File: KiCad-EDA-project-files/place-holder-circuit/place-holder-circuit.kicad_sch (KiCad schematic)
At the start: 4 parts

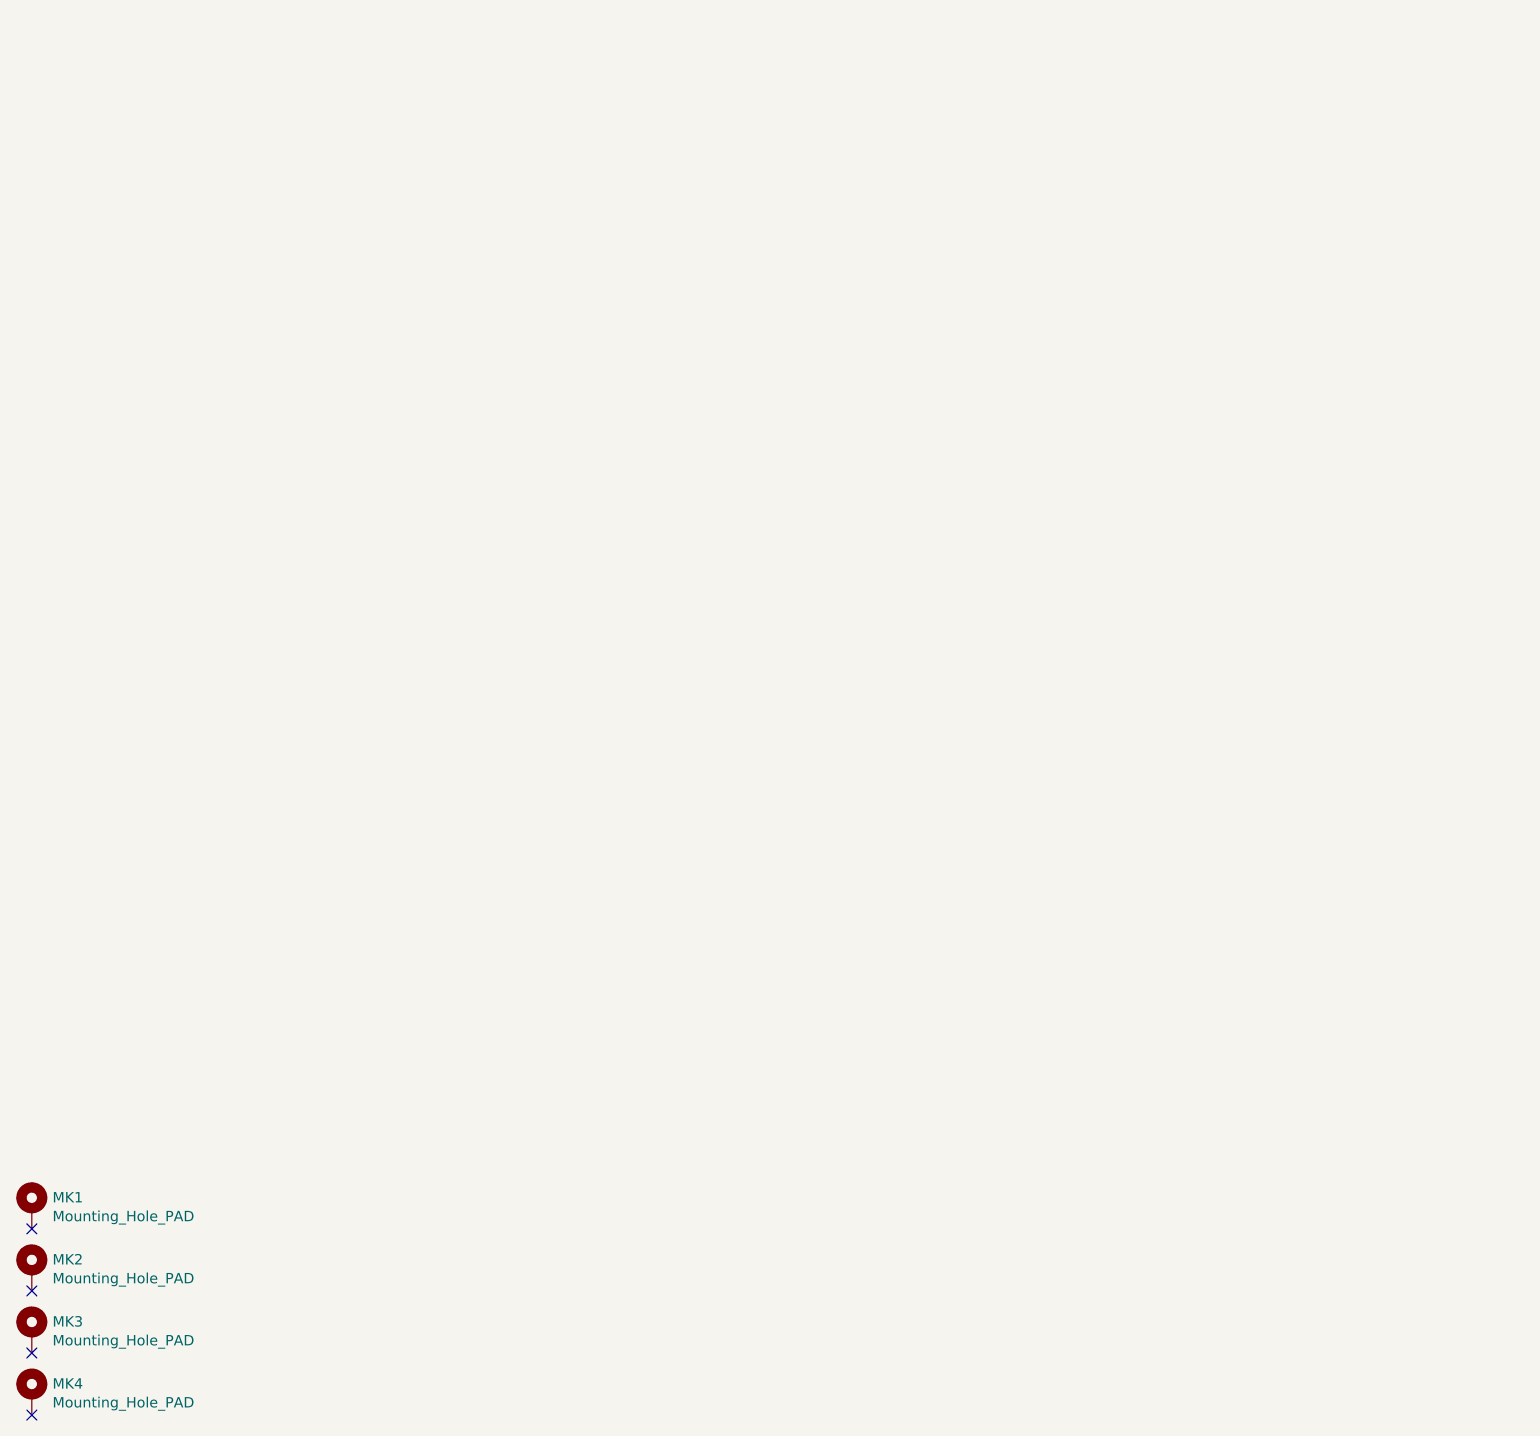
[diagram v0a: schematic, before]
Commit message: Created more project files. Added directory for programming libraries.
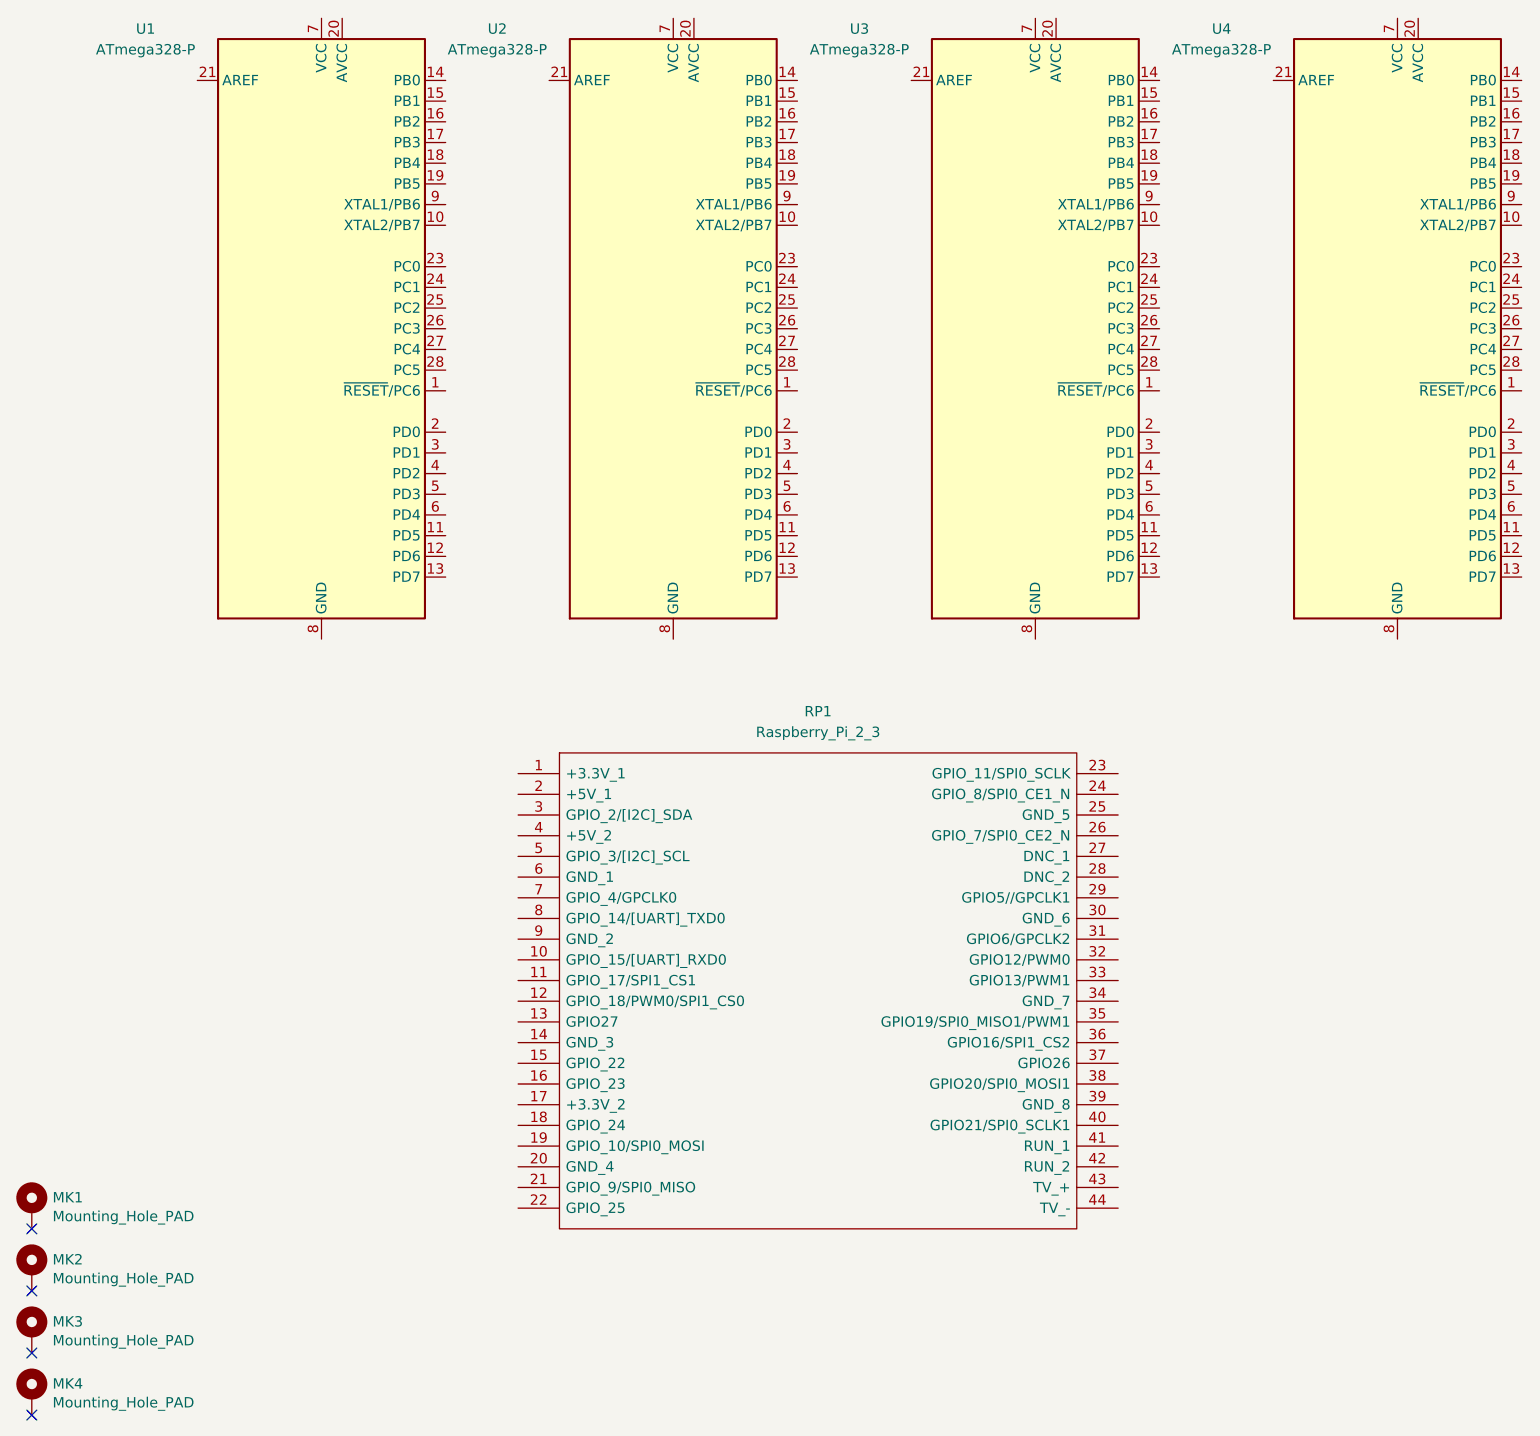
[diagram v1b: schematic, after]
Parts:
- added RP1: Raspberry_Pi_2_3, RASPBERRYPI, symbol Raspberry_Pi_2_or_3:Raspberry_Pi_2_3
- added U1, U2, U3, U4: ATmega328-P, Package_DIP:DIP-28_W7.62mm, symbol MCU_Microchip_ATmega:ATmega328-P
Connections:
- new net: U3.22 (GND), U3.8 (GND)
- new net: U1.22 (GND), U1.8 (GND)
- new net: U4.22 (GND), U4.8 (GND)
- new net: U2.22 (GND), U2.8 (GND)
